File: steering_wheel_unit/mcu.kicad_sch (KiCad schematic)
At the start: 38 parts, among them SW1 TL3305BF100QG, SW2 TL3305BF100QG, U1 STM32G491CCTx, U2 USBLC6-2P6, Y1 9HT7-32.768KDZF-T, Y2 ABM11W-24.0000MHZ-8-D1X-T3

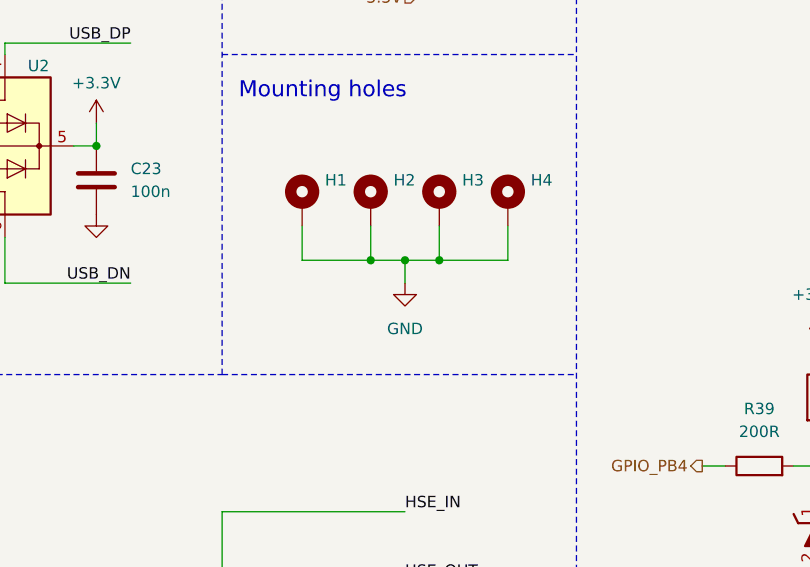
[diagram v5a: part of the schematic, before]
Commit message: Add more gnd vias
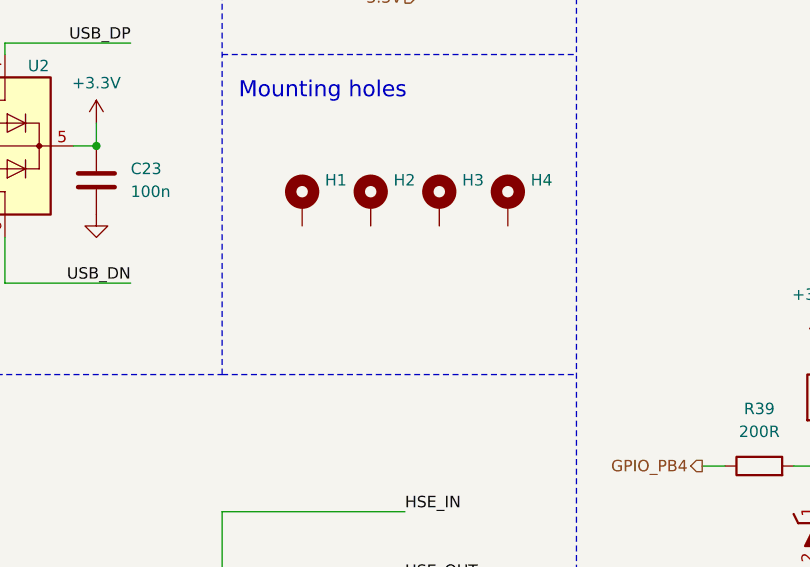
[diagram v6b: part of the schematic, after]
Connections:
- net GND: no longer H1.1, H2.1, H3.1, H4.1
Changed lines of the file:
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@@
 	)
 	(junction
-		(at 99.06 113.03)
-		(diameter 0)
-		(color 0 0 0 0)
-	)
-	(junction
 		(at 240.03 39.37)
 		(diameter 0)
@@
 	)
 	(junction
-		(at 102.87 113.03)
-		(diameter 0)
-		(color 0 0 0 0)
-	)
-	(junction
-		(at 106.68 113.03)
-		(diameter 0)
-		(color 0 0 0 0)
-	)
-	(junction
 		(at 219.71 25.4)
 		(diameter 0)
@@
 	(wire
 		(pts
-			(xy 114.3 113.03) (xy 114.3 109.22)
-		)
-		(stroke
-			(width 0)
-			(type default)
-		)
-	)
-	(wire
-		(pts
 			(xy 48.26 50.8) (xy 54.61 50.8)
 		)
@@
 	(wire
 		(pts
-			(xy 91.44 109.22) (xy 91.44 113.03)
-		)
-		(stroke
-			(width 0)
-			(type default)
-		)
-	)
-	(wire
-		(pts
 			(xy 92.71 179.07) (xy 92.71 177.8)
 		)
@@
 	(wire
 		(pts
-			(xy 106.68 109.22) (xy 106.68 113.03)
-		)
-		(stroke
-			(width 0)
-			(type default)
-		)
-	)
-	(wire
-		(pts
 			(xy 53.34 151.13) (xy 60.96 151.13)
 		)
@@
 	(wire
 		(pts
-			(xy 106.68 113.03) (xy 114.3 113.03)
-		)
-		(stroke
-			(width 0)
-			(type default)
-		)
-	)
-	(wire
-		(pts
 			(xy 175.26 100.33) (xy 193.04 100.33)
 		)
@@
 	(wire
 		(pts
-			(xy 102.87 113.03) (xy 106.68 113.03)
-		)
-		(stroke
-			(width 0)
-			(type default)
-		)
-	)
-	(wire
-		(pts
 			(xy 184.15 67.31) (xy 193.04 67.31)
 		)
@@
 	(wire
 		(pts
-			(xy 91.44 113.03) (xy 99.06 113.03)
-		)
-		(stroke
-			(width 0)
-			(type default)
-		)
-	)
-	(wire
-		(pts
 			(xy 222.25 54.61) (xy 222.25 50.8)
 		)
@@
 	(wire
 		(pts
-			(xy 102.87 115.57) (xy 102.87 113.03)
-		)
-		(stroke
-			(width 0)
-			(type default)
-		)
-	)
-	(wire
-		(pts
 			(xy 109.22 83.82) (xy 109.22 82.55)
 		)
@@
 	(wire
 		(pts
-			(xy 99.06 109.22) (xy 99.06 113.03)
-		)
-		(stroke
-			(width 0)
-			(type default)
-		)
-	)
-	(wire
-		(pts
 			(xy 162.56 123.19) (xy 162.56 124.46)
 		)
@@
 	(wire
 		(pts
-			(xy 99.06 113.03) (xy 102.87 113.03)
-		)
-		(stroke
-			(width 0)
-			(type default)
-		)
-	)
-	(wire
-		(pts
 			(xy 60.96 151.13) (xy 60.96 157.48)
 		)
@@
 					(unit 1)
 				)
-			)
-		)
-	)
-	(symbol
-		(lib_id "power:GND")
-		(at 102.87 115.57 0)
-		(unit 1)
-		(exclude_from_sim no)
-		(in_bom yes)
-		(on_board yes)
-		(dnp no)
-		(fields_autoplaced yes)
-		(property "Reference" "#PWR073"
-			(at 102.87 121.92 0)
-			(effects
-				(font
-					(size 1.27 1.27)
-				)
-				(hide yes)
-			)
-		)
-		(property "Value" "GND"
-			(at 102.87 120.65 0)
-			(effects
-				(font
-					(size 1.27 1.27)
-				)
-			)
-		)
-		(property "Footprint" ""
-			(at 102.87 115.57 0)
-			(effects
-				(font
-					(size 1.27 1.27)
-				)
-				(hide yes)
-			)
-		)
-		(property "Datasheet" ""
-			(at 102.87 115.57 0)
-			(effects
-				(font
-					(size 1.27 1.27)
-				)
-				(hide yes)
-			)
-		)
-		(property "Description" "Power symbol creates a global label with name \"GND\" , ground"
-			(at 102.87 115.57 0)
-			(effects
-				(font
-					(size 1.27 1.27)
-				)
-				(hide yes)
-			)
-		)
-		(pin "1"
-		)
-		(instances
-			(project "steering_wheel_unit"
-				(path "/b435671d-bfd7-4707-b36e-3eecb7fa1f89/49e3c9ae-cbf9-4f58-a1a3-484e0a637fd9"
-					(reference "#PWR073")
-					(unit 1)
-				)

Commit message: Add manufacturing
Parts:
- renumbered Z3 to Z1, Z4 to Z2
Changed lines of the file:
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@@
 		(dnp no)
 		(fields_autoplaced yes)
-		(property "Reference" "Z3"
-			(at 153.035 143.5099 90)
+		(property "Reference" "Z1"
+			(at 152.4 141.7319 90)
 			(effects
 				(font
@@
 		)
 		(property "Value" "MMSZ3V3T1G"
-			(at 153.035 146.0499 90)
+			(at 152.4 144.2719 90)
 			(effects
 				(font
@@
 			(project "steering_wheel_unit"
 				(path "/b435671d-bfd7-4707-b36e-3eecb7fa1f89/49e3c9ae-cbf9-4f58-a1a3-484e0a637fd9"
-					(reference "Z3")
+					(reference "Z1")
 					(unit 1)
 				)
@@
 		(dnp no)
 		(fields_autoplaced yes)
-		(property "Reference" "Z4"
-			(at 266.065 139.6999 90)
+		(property "Reference" "Z2"
+			(at 265.43 137.9219 90)
 			(effects
 				(font
@@
 		)
 		(property "Value" "MMSZ3V3T1G"
-			(at 266.065 142.2399 90)
+			(at 265.43 140.4619 90)
 			(effects
 				(font
@@
 			(project "steering_wheel_unit"
 				(path "/b435671d-bfd7-4707-b36e-3eecb7fa1f89/49e3c9ae-cbf9-4f58-a1a3-484e0a637fd9"
-					(reference "Z4")
-					(unit 1)
-				)
+					(reference "Z2")
+					(unit 1)
+				)
